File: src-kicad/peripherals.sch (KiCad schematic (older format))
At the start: 31 parts, among them J15 1x4_male_pin_Header_2.54mm, J16 1x4_male_pin_Header_2.54mm, J17 1x4_male_pin_Header_2.54mm, SW1 Switch, SW2 Switch, U7 ADS7924

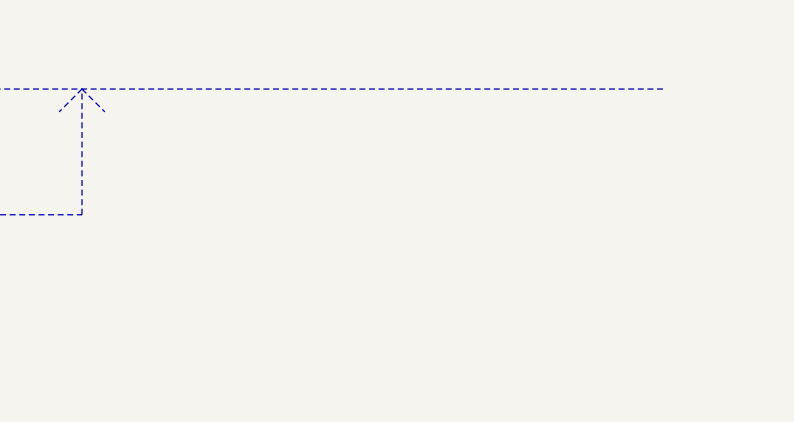
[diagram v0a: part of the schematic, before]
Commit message: Kicad schematic: added fpgawars logo and CC-BY-SA to all the sheets
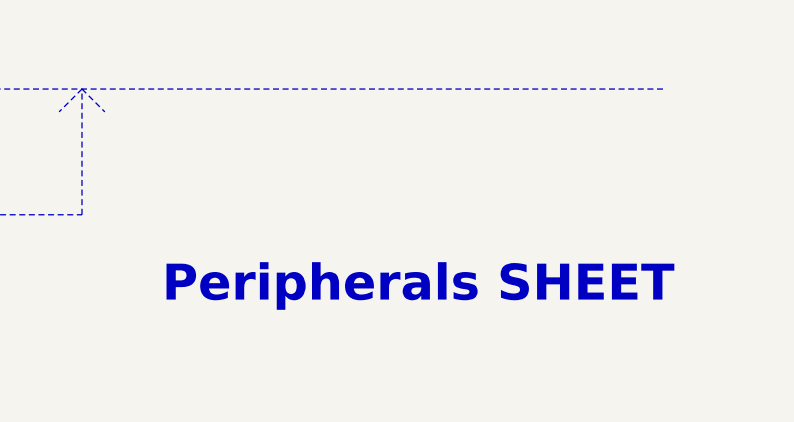
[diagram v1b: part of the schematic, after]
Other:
- note added: "Peripherals SHEET"

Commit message: pcb migration: initial commit
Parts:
- D2: footprint (none) -> Icezum:LED_0603
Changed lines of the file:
@@
 F 0 "D2" H 2440 1300 47  0000 L BNN
 F 1 "Yellow" H 2450 1210 47  0000 L BNN
-F 2 "" H 1950 1200 60  0000 C CNN
+F 2 "Icezum:LED_0603" H 1950 1200 60  0001 C CNN
 F 3 "" H 1950 1200 60  0000 C CNN
 	1    1950 1200
@@
 F3 F0 1D 79 17 0B BC D0 AE 96 03 B8 3F 0C 6D B8 A2 A8 0B 16 2C 58 B0 60 C1 82 05 0B 16 2C 58 B0
 60 C1 82 05 0B 16 2C 58 B0 E0 7F 81 FF 00 64 C5 01 8A 14 5C 86 66 00 00 00 00 49 45 4E 44 AE 42
-60 82 46
+60 82 0A
 EndData
 $EndBitmap

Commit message: Kicad pcb migration: pcb edges added
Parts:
- D3, D4, D5, D6, D7, D8, D9: footprint (none) -> Icezum:LED_0603
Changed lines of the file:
@@
 EESchema Schematic File Version 2
 LIBS:icezum
+LIBS:icezum-cache
 EELAYER 25 0
 EELAYER END
@@
 F 0 "D3" H 2440 1700 47  0000 L BNN
 F 1 "Yellow" H 2450 1610 47  0000 L BNN
-F 2 "" H 1950 1600 60  0000 C CNN
+F 2 "Icezum:LED_0603" H 1950 1600 60  0001 C CNN
 F 3 "" H 1950 1600 60  0000 C CNN
 	1    1950 1600
@@
 F 0 "D4" H 2440 2100 47  0000 L BNN
 F 1 "Yellow" H 2450 2010 47  0000 L BNN
-F 2 "" H 1950 2000 60  0000 C CNN
+F 2 "Icezum:LED_0603" H 1950 2000 60  0001 C CNN
 F 3 "" H 1950 2000 60  0000 C CNN
 	1    1950 2000
@@
 F 0 "D5" H 2440 2500 47  0000 L BNN
 F 1 "Yellow" H 2450 2410 47  0000 L BNN
-F 2 "" H 1950 2400 60  0000 C CNN
+F 2 "Icezum:LED_0603" H 1950 2400 60  0001 C CNN
 F 3 "" H 1950 2400 60  0000 C CNN
 	1    1950 2400
@@
 F 0 "D6" H 2440 2900 47  0000 L BNN
 F 1 "Yellow" H 2450 2810 47  0000 L BNN
-F 2 "" H 1950 2800 60  0000 C CNN
+F 2 "Icezum:LED_0603" H 1950 2800 60  0001 C CNN
 F 3 "" H 1950 2800 60  0000 C CNN
 	1    1950 2800
@@
 F 0 "D7" H 2440 3300 47  0000 L BNN
 F 1 "Yellow" H 2450 3210 47  0000 L BNN
-F 2 "" H 1950 3200 60  0000 C CNN
+F 2 "Icezum:LED_0603" H 1950 3200 60  0001 C CNN
 F 3 "" H 1950 3200 60  0000 C CNN
 	1    1950 3200
@@
 F 0 "D8" H 2440 3700 47  0000 L BNN
 F 1 "Yellow" H 2450 3610 47  0000 L BNN
-F 2 "" H 1950 3600 60  0000 C CNN
+F 2 "Icezum:LED_0603" H 1950 3600 60  0001 C CNN
 F 3 "" H 1950 3600 60  0000 C CNN
 	1    1950 3600
@@
 F 0 "D9" H 2440 4100 47  0000 L BNN
 F 1 "Yellow" H 2450 4010 47  0000 L BNN
-F 2 "" H 1950 4000 60  0000 C CNN
+F 2 "Icezum:LED_0603" H 1950 4000 60  0001 C CNN
 F 3 "" H 1950 4000 60  0000 C CNN
 	1    1950 4000
@@
 F3 F0 1D 79 17 0B BC D0 AE 96 03 B8 3F 0C 6D B8 A2 A8 0B 16 2C 58 B0 60 C1 82 05 0B 16 2C 58 B0
 60 C1 82 05 0B 16 2C 58 B0 E0 7F 81 FF 00 64 C5 01 8A 14 5C 86 66 00 00 00 00 49 45 4E 44 AE 42
-60 82 0A
+60 82 2E
 EndData
 $EndBitmap

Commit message: Kicad PCB migration: R17 and R18 added, with 3D models
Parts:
- R17, R18: footprint (none) -> Icezum:R_Array_Convex_4x0603
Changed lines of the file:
@@
 F 0 "R17" H 1550 1300 47  0000 C CNN
 F 1 "270R±5% 0.063w" H 1550 1090 47  0000 C CNN
-F 2 "" H 1250 1200 79  0000 C CNN
+F 2 "Icezum:R_Array_Convex_4x0603" H 1250 1200 79  0001 C CNN
 F 3 "" H 1250 1200 79  0000 C CNN
 	1    1250 1200
@@
 F 0 "R17" H 1550 1700 47  0000 C CNN
 F 1 "270R±5% 0.063w" H 1550 1490 47  0000 C CNN
-F 2 "" H 1250 1600 79  0000 C CNN
+F 2 "Icezum:R_Array_Convex_4x0603" H 1250 1600 79  0001 C CNN
 F 3 "" H 1250 1600 79  0000 C CNN
 	2    1250 1600
@@
 F 0 "R17" H 1550 2100 47  0000 C CNN
 F 1 "270R±5% 0.063w" H 1550 1890 47  0000 C CNN
-F 2 "" H 1250 2000 79  0000 C CNN
+F 2 "Icezum:R_Array_Convex_4x0603" H 1250 2000 79  0001 C CNN
 F 3 "" H 1250 2000 79  0000 C CNN
 	3    1250 2000
@@
 F 0 "R17" H 1550 2500 47  0000 C CNN
 F 1 "270R±5% 0.063w" H 1550 2290 47  0000 C CNN
-F 2 "" H 1250 2400 79  0000 C CNN
+F 2 "Icezum:R_Array_Convex_4x0603" H 1250 2400 79  0001 C CNN
 F 3 "" H 1250 2400 79  0000 C CNN
 	4    1250 2400
@@
 F 0 "R18" H 1550 2900 47  0000 C CNN
 F 1 "270R±5% 0.063w" H 1550 2690 47  0000 C CNN
-F 2 "" H 1250 2800 79  0000 C CNN
+F 2 "Icezum:R_Array_Convex_4x0603" H 1250 2800 79  0001 C CNN
 F 3 "" H 1250 2800 79  0000 C CNN
 	1    1250 2800
@@
 F 0 "R18" H 1550 3300 47  0000 C CNN
 F 1 "270R±5% 0.063w" H 1550 3090 47  0000 C CNN
-F 2 "" H 1250 3200 79  0000 C CNN
+F 2 "Icezum:R_Array_Convex_4x0603" H 1250 3200 79  0001 C CNN
 F 3 "" H 1250 3200 79  0000 C CNN
 	2    1250 3200
@@
 F 0 "R18" H 1550 3700 47  0000 C CNN
 F 1 "270R±5% 0.063w" H 1550 3490 47  0000 C CNN
-F 2 "" H 1250 3600 79  0000 C CNN
+F 2 "Icezum:R_Array_Convex_4x0603" H 1250 3600 79  0001 C CNN
 F 3 "" H 1250 3600 79  0000 C CNN
 	3    1250 3600
@@
 F 0 "R18" H 1550 4100 47  0000 C CNN
 F 1 "270R±5% 0.063w" H 1550 3890 47  0000 C CNN
-F 2 "" H 1250 4000 79  0000 C CNN
+F 2 "Icezum:R_Array_Convex_4x0603" H 1250 4000 79  0001 C CNN
 F 3 "" H 1250 4000 79  0000 C CNN
 	4    1250 4000
@@
 F3 F0 1D 79 17 0B BC D0 AE 96 03 B8 3F 0C 6D B8 A2 A8 0B 16 2C 58 B0 60 C1 82 05 0B 16 2C 58 B0
 60 C1 82 05 0B 16 2C 58 B0 E0 7F 81 FF 00 64 C5 01 8A 14 5C 86 66 00 00 00 00 49 45 4E 44 AE 42
-60 82 2E
+60 82 00
 EndData
 $EndBitmap

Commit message: Kicad pcb migration: User switches added to the PCB
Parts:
- SW1, SW2: footprint (none) -> Icezum:SW_SMD_60X3.8
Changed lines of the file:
@@
 F 0 "SW1" H 4550 1450 60  0000 L BNN
 F 1 "Switch" H 4550 1150 60  0000 L BNN
-F 2 "" H 4350 1300 60  0000 C CNN
+F 2 "Icezum:SW_SMD_60X3.8" H 4350 1300 60  0001 C CNN
 F 3 "" H 4350 1300 60  0000 C CNN
 	1    4350 1300
@@
 F 0 "SW2" H 4550 2350 60  0000 L BNN
 F 1 "Switch" H 4550 2050 60  0000 L BNN
-F 2 "" H 4350 2200 60  0000 C CNN
+F 2 "Icezum:SW_SMD_60X3.8" H 4350 2200 60  0001 C CNN
 F 3 "" H 4350 2200 60  0000 C CNN
 	1    4350 2200
@@
 B8 D2 A5 D0 D0 88 43 83 08 6C BD D2 A5 D0 D0 88 C3 36 11 89 E7 80 EE 2B 5D 12 0D 8D 28 1C 42 E0
 0D 11 99 76 E0 6E E0 E3 2B 5D 22 0D 8D 71 EC 07 1E E7 1B 7C F8 FF 01 FB D1 C8 6E 4C 03 14 F4 00
-00 00 00 49 45 4E 44 AE 42 60 82 00
+00 00 00 49 45 4E 44 AE 42 60 82 09
 EndData
 $EndBitmap
